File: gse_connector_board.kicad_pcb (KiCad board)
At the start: 2 copper layers, 50 x 20 mm, 19 parts, among them J1 arming_connector, J2 gse_com_connector, J3 chg_connector, U4 L7805, U7 ISO1044BD, U9 MCP2562-E-SN

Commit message: wip
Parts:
- removed BUS1: 43045-0800, Connector_Molex:Molex_Micro-Fit_3.0_43045-0800_2x04_P3.00mm_Horizontal
- removed H3: MountingHole_Pad, MountingHole:MountingHole_3.2mm_M3_DIN965_Pad
- added J4: Conn_02x03_Top_Bottom, Connector_Molex:Molex_Micro-Fit_3.0_43045-0600_2x03_P3.00mm_Horizontal, F.Cu at (121.4, 66.3)
- added J5: Conn_02x02_Top_Bottom, Connector_Molex:Molex_Micro-Fit_3.0_43045-0400_2x02_P3.00mm_Horizontal, F.Cu at (155.3, 66.0)
- JP4: footprint Connector_PinHeader_1.27mm:PinHeader_1x02_P1.27mm_Vertical -> Jumper:SolderJumper-2_P1.3mm_Bridged_RoundedPad1.0x1.5mm
- moved H2 42.9 mm to (120.4, 78.6)
- moved J2 11.3 mm to (149.0, 72.1)
- moved J3 10.6 mm to (136.7, 72.0)
- moved C23 9.34 mm to (150.2, 64.9)
- moved C24 8.57 mm to (150.2, 61.5)
- moved U7 8.48 mm to (145.4, 62.6)
- moved C22 7.23 mm to (142.6, 59.1), turned to 180 degrees
- moved JP4 6.91 mm to (133.6, 58.6), turned to 180 degrees
- moved U9 6.58 mm to (136.6, 62.6)
- moved R22 6.39 mm to (132.1, 61.1)
- moved C28 6.38 mm to (149.5, 58.8)
- moved J1 6.33 mm to (165.4, 72.2)
- moved C29 5.90 mm to (146.5, 58.9)
- moved H1 5.88 mm to (166.6, 60.0)
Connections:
- J1 pad 1: supply -> main_voltage
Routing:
- net CHG: track 0.00 -> 23.0 mm
- net main_voltage: track 17.0 -> 30.6 mm
- net GND: track 30.8 -> 36.3 mm
- net Net-(U7-TXD): track 6.58 -> 2.77 mm
- net Net-(U7-RXD): track 6.58 -> 2.77 mm
- net +5V: track 58.6 -> 56.5 mm
- added copper zone on B.Cu, net GND
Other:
- board size 50 x 20 mm -> 53 x 25 mm
- board text added: "Arming"
- board text added: "CHG"
- board text added: "GSE com"
- board text added: "arm"

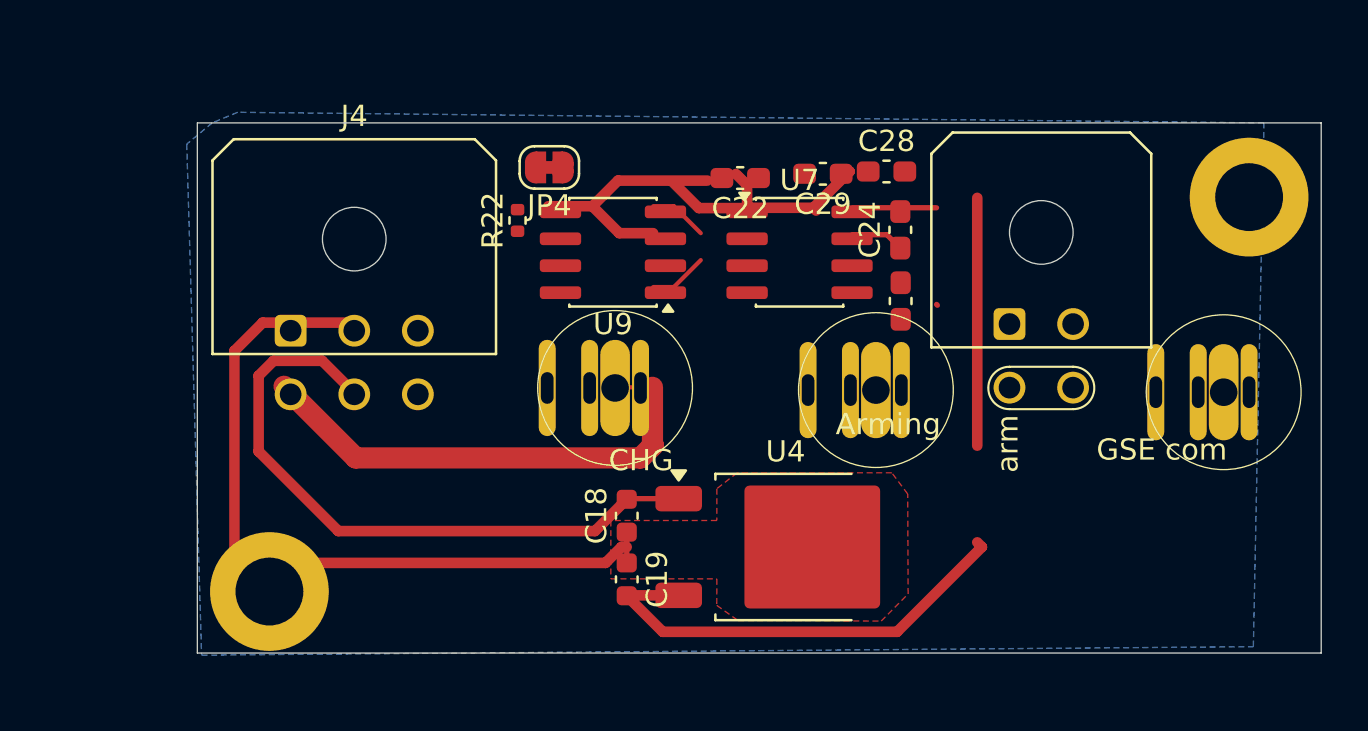
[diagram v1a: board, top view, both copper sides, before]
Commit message: Add files via upload
changed footprint of agnetic connector, finished routing and layout of connector board
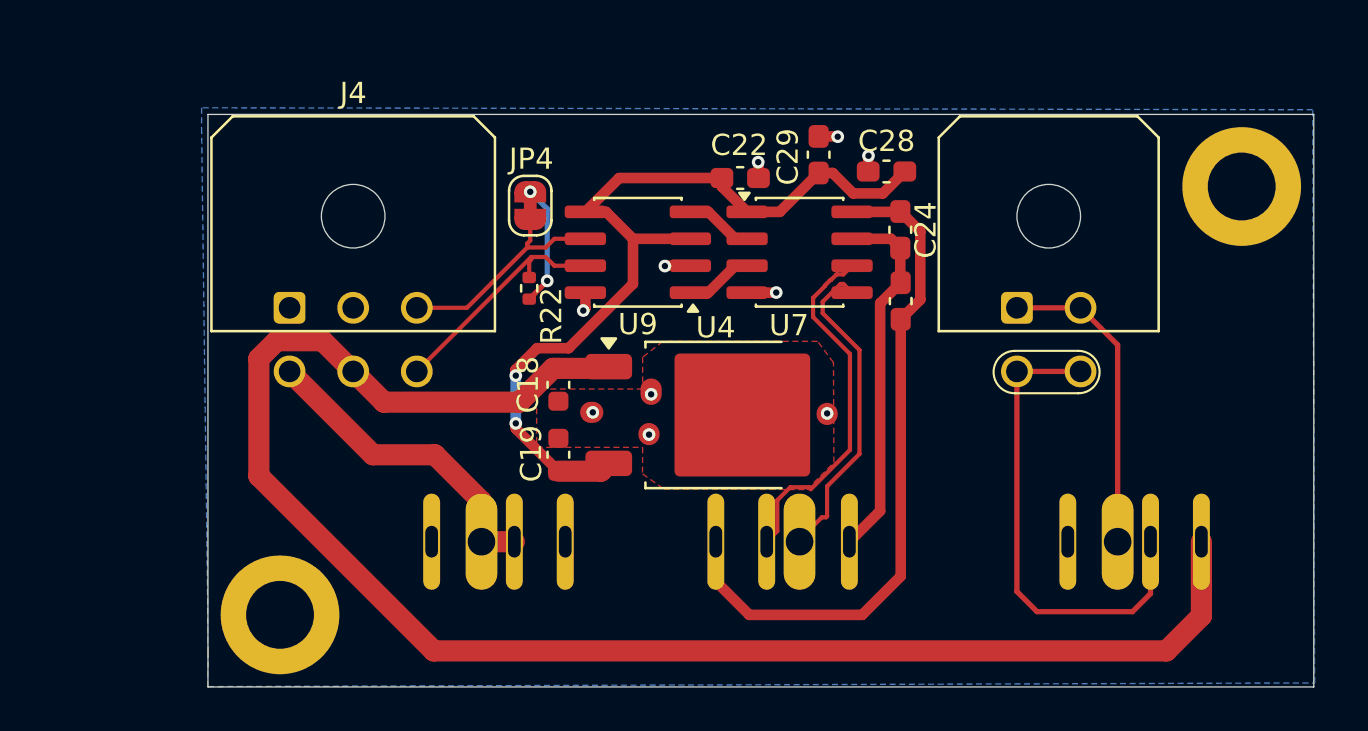
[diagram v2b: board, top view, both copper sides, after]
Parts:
- J1, J2, J3: footprint custom_parts:4_pin_mag_con -> custom_parts:4_pin_mag_con_new; moved to B.Cu
- moved J3 9.60 mm to (130.4, 79.2), turned to 180 degrees
- moved J1 8.64 mm to (160.4, 79.2), turned to 180 degrees
- moved U4 7.04 mm to (141.4, 70.3)
- moved C18 6.97 mm to (134.0, 68.8)
- moved C19 6.70 mm to (134.0, 72.2)
- moved J2 3.78 mm to (145.4, 73.2)
- moved R22 3.25 mm to (132.7, 64.3), turned to -90 degrees
- moved JP4 2.01 mm to (132.7, 60.4), turned to 90 degrees
- moved H2 1.21 mm to (120.9, 79.7)
- moved U9 1.18 mm to (137.8, 62.6)
- moved J4 1.08 mm to (121.3, 65.2)
- moved C29 0.92 mm to (146.3, 58.0), turned to -90 degrees
- moved J5 0.84 mm to (155.7, 65.2)
- moved H1 0.61 mm to (166.2, 59.5)
- turned C23 to -90 degrees
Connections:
- net CAN_ext_H renamed CAN_ext+
- net CAN_ext_L renamed CAN_ext-
- C23 pad 1: GNDEXT -> GND_EXT
- JP4 pad 1: CAN_1_L -> CAN_1-
- R22 pad 1: CAN_1_H -> CAN_1+
- U9 pad 6: CAN_1_L -> CAN_1-
- U9 pad 7: CAN_1_H -> CAN_1+
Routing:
- net main_voltage: track 30.6 -> 76.3 mm
- net GND: track 36.3 -> 6.33 mm, vias 0 -> 10
- net +V_EXT: track 4.04 -> 32.3 mm
- net arm: track 0.00 -> 22.9 mm
- net CAN_ext-: track 0.00 -> 17.5 mm
- net CAN_ext+: track 0.00 -> 17.0 mm
- net +5V: track 56.5 -> 41.2 mm, vias 0 -> 2
- net GND_EXT: track 2.54 -> 17.3 mm
- net disarm: track 0.00 -> 14.8 mm
- net CAN_1+: track 0.00 -> 11.4 mm
- net CAN_1-: track 0.00 -> 10.7 mm
- net CHG: track 23.0 -> 15.0 mm
- net Net-(JP4-B): track 0.00 -> 5.74 mm, vias 0 -> 2
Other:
- board size 53 x 25 mm -> 52.2 x 27 mm
- board text removed: "arm"

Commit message: Add files via upload
added rounded corners
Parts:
- moved J4 0.11 mm to (121.2, 65.2)
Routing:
- net CHG: track 15.0 -> 13.8 mm
- net main_voltage: track 76.3 -> 77.5 mm
- added copper zone on F.Cu, net CHG
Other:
- outline, holes or cut-outs redrawn
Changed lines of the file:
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@@
 	(footprint "Connector_Molex:Molex_Micro-Fit_3.0_43045-0600_2x03_P3.00mm_Horizontal"
 		(layer "F.Cu")
-		(at 121.35 65.22)
+		(at 121.25 65.185)
 		(descr "Molex Micro-Fit 3.0 Connector System, 43045-0600 (alternative finishes: 43045-060x), 3 Pins per row (https://www.molex.com/pdm_docs/sd/430450201_sd.pdf)")
 		(tags "connector Molex Micro-Fit_3.0 horizontal")
@@
 		(layer "Dwgs.User")
 	)
-	(gr_rect
-		(start 117.5 56.1)
-		(end 169.65 83.1)
+	(gr_arc
+		(start 117.5 58.1)
+		(mid 118.085786 56.685786)
+		(end 119.5 56.1)
+		(stroke
+			(width 0.05)
+			(type default)
+		)
+		(layer "Edge.Cuts")
+	)
+	(gr_line
+		(start 117.5 81.1)
+		(end 117.5 58.1)
+		(stroke
+			(width 0.05)
+			(type default)
+		)
+		(layer "Edge.Cuts")
+	)
+	(gr_line
+		(start 119.5 56.1)
+		(end 167.65 56.1)
+		(stroke
+			(width 0.05)
+			(type default)
+		)
+		(layer "Edge.Cuts")
+	)
+	(gr_arc
+		(start 119.5 83.1)
+		(mid 118.085786 82.514214)
+		(end 117.5 81.1)
+		(stroke
+			(width 0.05)
+			(type default)
+		)
+		(layer "Edge.Cuts")
+	)
+	(gr_arc
+		(start 167.65 56.1)
+		(mid 169.064214 56.685786)
+		(end 169.65 58.1)
+		(stroke
+			(width 0.05)
+			(type default)
+		)
+		(layer "Edge.Cuts")
+	)
+	(gr_line
+		(start 167.65 83.1)
+		(end 119.5 83.1)
+		(stroke
+			(width 0.05)
+			(type default)
+		)
+		(layer "Edge.Cuts")
+	)
+	(gr_line
+		(start 169.65 58.1)
+		(end 169.65 81.1)
+		(stroke
+			(width 0.05)
+			(type default)
+		)
+		(layer "Edge.Cuts")
+	)
+	(gr_arc
+		(start 169.65 81.1)
+		(mid 169.064214 82.514214)
+		(end 167.65 83.1)
 		(stroke
 			(width 0.05)
 			(type default)
 		)
-		(fill no)
 		(layer "Edge.Cuts")
 	)
@@
 	)
 	(segment
-		(start 119.9 67.61939)
-		(end 119.9 73.15)
-		(width 1)
-		(layer "F.Cu")
-		(net "main_voltage")
-	)
-	(segment
-		(start 128.15 81.4)
-		(end 162.7 81.4)
+		(start 122.75 66.745)
+		(end 119.805 66.745)
 		(width 1)
 		(layer "F.Cu")
@@
 	)
 	(segment
-		(start 120.74939 66.77)
-		(end 119.9 67.61939)
+		(start 124.2 68.195)
+		(end 122.75 66.745)
 		(width 1)
 		(layer "F.Cu")
@@
 	(segment
 		(start 124.35 68.22)
-		(end 122.9 66.77)
+		(end 125.8 69.67)
 		(width 1)
 		(layer "F.Cu")
@@
 	)
 	(segment
-		(start 124.35 68.22)
-		(end 125.8 69.67)
+		(start 128.15 81.4)
+		(end 162.7 81.4)
 		(width 1)
 		(layer "F.Cu")
@@
 	)
 	(segment
+		(start 119 72.25)
+		(end 128.15 81.4)
+		(width 1)
+		(layer "F.Cu")
+		(net "main_voltage")
+	)
+	(segment
 		(start 162.7 81.4)
 		(end 164.35 79.75)
@@
 	)
 	(segment
-		(start 119.9 73.15)
-		(end 128.15 81.4)
+		(start 164.35 79.75)
+		(end 164.35 76.25)
 		(width 1)
 		(layer "F.Cu")
@@
 	)
 	(segment
-		(start 122.9 66.77)
-		(end 120.74939 66.77)
+		(start 119 67.55)
+		(end 119 72.25)
 		(width 1)
 		(layer "F.Cu")
@@
 	)
 	(segment
-		(start 125.8 69.67)
-		(end 132.18 69.67)
+		(start 119.805 66.745)
+		(end 119 67.55)
 		(width 1)
 		(layer "F.Cu")
@@
 	)
 	(segment
-		(start 136.321959 68.075)
-		(end 136.401959 67.995)
+		(start 125.8 69.67)
+		(end 132.18 69.67)
 		(width 1)
 		(layer "F.Cu")
@@
 	)
 	(segment
-		(start 164.35 79.75)
-		(end 164.35 76.25)
+		(start 136.321959 68.075)
+		(end 136.401959 67.995)
 		(width 1)
 		(layer "F.Cu")
@@
 	)
 	(segment
-		(start 128.2 72.15)
-		(end 130.4 74.35)
+		(start 121.35 68.22)
+		(end 124.88 71.75)
 		(width 1)
 		(layer "F.Cu")
@@
 	)
 	(segment
-		(start 125.28 72.15)
-		(end 128.2 72.15)
+		(start 124.88 71.75)
+		(end 129.675 71.75)
 		(width 1)
 		(layer "F.Cu")
@@
 	)
 	(segment
-		(start 130.4 76.25)
-		(end 131.95 76.25)
-		(width 1)
-		(layer "F.Cu")
-		(net "CHG")
-	)
-	(segment
-		(start 121.35 68.22)
-		(end 125.28 72.15)
+		(start 129.675 71.75)
+		(end 131.15 73.225)
 		(width 1)
 		(layer "F.Cu")
@@
 			)
 		)
+	)
+	(zone
+		(net "CHG")
+		(layer "F.Cu")
+		(hatch edge 0.5)
+		(priority 2)
+		(connect_pads
+			(clearance 0.5)
+		)
+		(min_thickness 0.25)
+		(fill yes
+			(thermal_gap 0.5)
+			(thermal_bridge_width 0.5)
+			(island_removal_mode 0)
+		)
+		(polygon
+			(pts
+				(xy 129.175 73.175) (xy 129.15 79.025) (xy 133.025 79) (xy 132.975 73.175)
+			)
+		)

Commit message: Add files via upload
Added Silkscreen and Testpoints for CAN
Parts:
- added CAN+: TestPoint, TestPoint:TestPoint_Pad_1.0x1.0mm, B.Cu at (131.2, 65.0)
- added CAN-: TestPoint, TestPoint:TestPoint_Pad_1.0x1.0mm, B.Cu at (131.2, 63.0)
- added G***: LOGO, frodo_io_module:rapid_logo, B.Cu at (133.2, 58.4)
- added RXD: TestPoint, TestPoint:TestPoint_Pad_1.0x1.0mm, B.Cu at (142.8, 63.5)
- added TP CAN_ext+: TestPoint, TestPoint:TestPoint_Pad_1.0x1.0mm, B.Cu at (146.8, 67.1)
- added TPCAN_ext-: TestPoint, TestPoint:TestPoint_Pad_1.0x1.0mm, B.Cu at (148.6, 69.1)
- added TXD: TestPoint, TestPoint:TestPoint_Pad_1.0x1.0mm, B.Cu at (142.8, 61.4)
- renumbered U4 to Ue1
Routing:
- net Net-(U7-TXD): track 3.20 -> 3.73 mm, vias 0 -> 1
- net GND: track 6.33 -> 6.83 mm
- net CAN_1+: track 11.4 -> 11.8 mm, vias 0 -> 1
- net CAN_1-: track 10.7 -> 11.1 mm, vias 0 -> 1
- net CAN_ext+: track 17.0 -> 17.3 mm, vias 0 -> 1
- net Net-(U7-RXD): track 3.20 -> 3.45 mm, vias 0 -> 1
- net CAN_ext-: track 17.5 -> 17.8 mm, vias 0 -> 1
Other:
- board text added: "Arm"
- board text added: "CAN+"
- board text added: "CAN+_ext"
- board text added: "CAN-"
- board text added: "CAN-_ext"
- board text added: "Disarm"
- board text added: "GND"
- board text added: "GND_ext"
- board text added: "GSE Connectorboard"
- board text added: "J5"
- board text added: "JLCJLCJLCJLC"
- board text added: "Main Voltage"
- board text added: "V+_ext"
- board text added: "rev1"

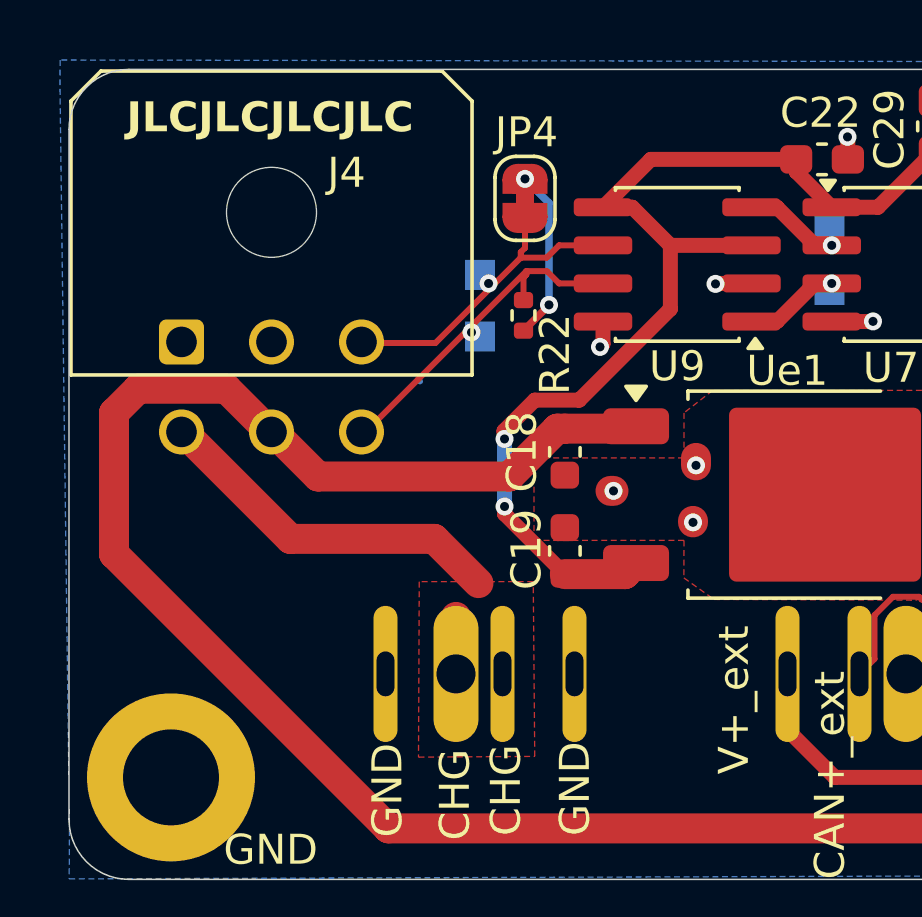
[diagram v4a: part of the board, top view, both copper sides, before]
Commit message: Add files via upload
excluded Molex connectors from BOM and put in DNP.
added Testpoints for 5V, main voltage and Charging
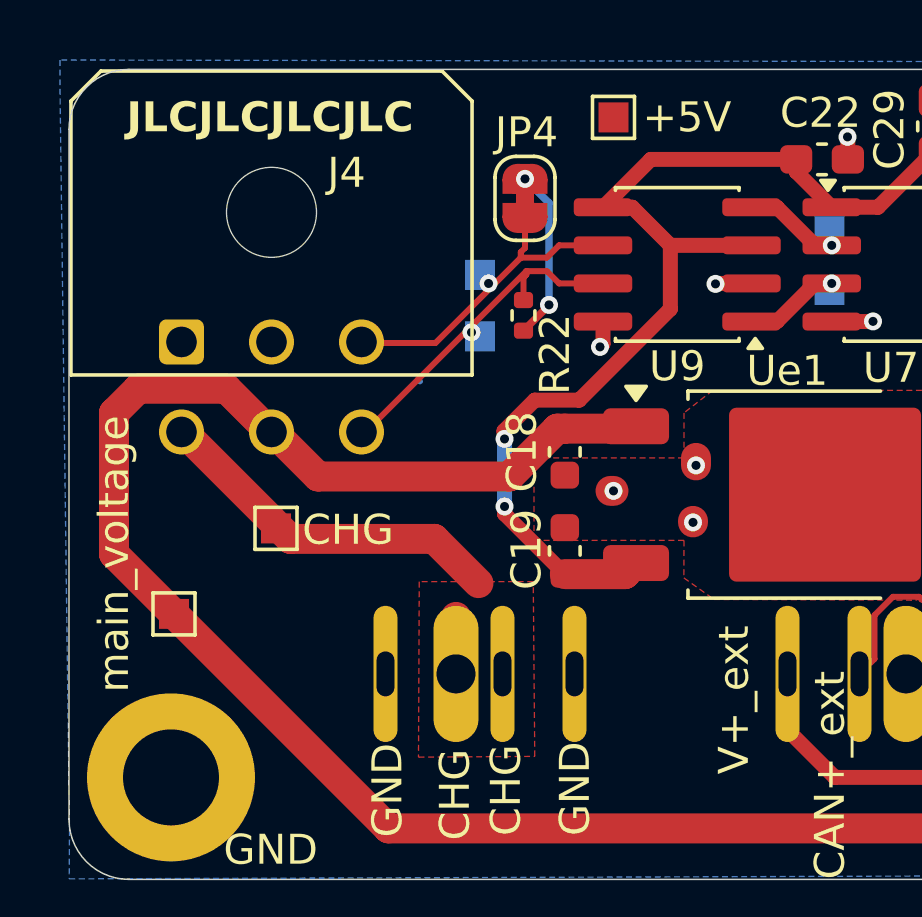
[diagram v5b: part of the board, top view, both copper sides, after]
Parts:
- added +5V: TestPoint, TestPoint:TestPoint_Pad_1.0x1.0mm, F.Cu at (135.7, 57.7)
- added CHG: TestPoint, TestPoint:TestPoint_Pad_1.0x1.0mm, F.Cu at (124.4, 71.4)
- added main_voltage: TestPoint, TestPoint:TestPoint_Pad_1.0x1.0mm, F.Cu at (121.0, 74.2)
- TP3: renamed from TP CAN_ext+
- renumbered CAN+ to TP1, CAN- to TP2, TPCAN_ext- to TP4, TXD to TP5, RXD to TP6

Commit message: Add files via upload
changed silkscreen
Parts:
- renumbered TP1 to CAN+, TP2 to CAN-, TP3 to CAN_ext+, TP4 to CAN_ext-, TP6 to RXD, TP5 to TXD, main_voltage to v_main
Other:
- board text added: "v_main"
- board text removed: "Main Voltage"

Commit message: final silkscreen improvements and small fixes
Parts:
- removed +5V, CAN+, CAN-, CAN_ext+, CAN_ext-, CHG, RXD, TXD, v_main: TestPoint, TestPoint:TestPoint_Pad_1.0x1.0mm
- added TP1: TestPoint, TestPoint:TestPoint_Pad_D1.0mm, B.Cu at (130.0, 66.0)
- added TP2: TestPoint, TestPoint:TestPoint_Pad_D1.0mm, B.Cu at (129.5, 62.0)
- added TP3: TestPoint, TestPoint:TestPoint_Pad_D1.0mm, B.Cu at (145.9, 67.3)
- added TP4: TestPoint, TestPoint:TestPoint_Pad_D1.0mm, B.Cu at (148.7, 66.4)
- added TP5: TestPoint, TestPoint:TestPoint_Pad_D1.0mm, B.Cu at (139.5, 60.2)
- added TP6: TestPoint, TestPoint:TestPoint_Pad_D1.0mm, B.Cu at (141.6, 65.9)
- added TP7: TestPoint, TestPoint:TestPoint_Pad_D1.0mm, F.Cu at (137.6, 75.2)
- C18, C19: footprint Capacitor_SMD:C_0603_1608Metric -> Capacitor_SMD:C_0603_1608Metric_Pad1.08x0.95mm_HandSolder
- R22: footprint Resistor_SMD:R_0402_1005Metric -> Resistor_SMD:R_0603_1608Metric_Pad0.98x0.95mm_HandSolder
- moved JP4 2.78 mm to (134.1, 58.0), turned to 180 degrees
- moved G*** 0.92 mm to (132.9, 59.2)
- moved C23 0.74 mm to (150.7, 65.4)
- moved R22 0.71 mm to (132.8, 65.0)
- moved C22 0.55 mm to (142.6, 58.5)
- moved C24 0.55 mm to (150.7, 61.5)
- moved J4 0.51 mm to (121.8, 65.3)
- moved C18 0.30 mm to (133.7, 68.8)
- moved C19 0.30 mm to (133.7, 72.2)
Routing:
- net +5V: track 41.2 -> 47.3 mm
- net CAN_1-: track 11.1 -> 14.9 mm
- net CAN_ext-: track 17.8 -> 14.0 mm
- net Net-(JP4-B): track 5.74 -> 9.31 mm
- net +V_EXT: track 32.3 -> 30.2 mm
- net CAN_1+: track 11.8 -> 13.7 mm
- net Net-(U7-RXD): track 3.45 -> 5.04 mm
- net Net-(U7-TXD): track 3.73 -> 5.04 mm
- net CHG: track 13.8 -> 14.9 mm
- net CAN_ext+: track 17.3 -> 16.7 mm
- net GND: track 6.83 -> 6.94 mm, vias 10 -> 101
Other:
- board text added: "+"
- board text added: "+5V"
- board text added: "-"
- board text added: "120Ω"
- board text added: "CAN"
- board text added: "CAN_ext"
- board text added: "CANext"
- board text added: "GSE"
- board text added: "RX->TX"
- board text added: "TX->RX"
- board text added: "Vchg"
- board text added: "Vmain"
- board text removed: "Arming"
- board text removed: "CAN+_ext"
- board text removed: "CAN-_ext"
- board text removed: "GSE com"
- board text removed: "J5"
- board text removed: "v_main"
